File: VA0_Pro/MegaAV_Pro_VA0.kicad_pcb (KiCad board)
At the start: 4 copper layers, 50 x 50 mm, 180 parts, among them CN1 MD-90SM_MD2, P1 SMD_Conn_01x01, U1 CD4070, U2 74HCT123, U3 TS924, U4 THS7374, U5 ICS501, U6 TS922, U7 TS924, U8 AD723, U9 NCV8114ASN250T1G

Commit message: MegaAV VA0 CE PCBA updates
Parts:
- U6: footprint Package_SO:TSSOP-8_4.4x3mm_P0.65mm -> Package_SO:SO-8_3.9x4.9mm_P1.27mm
- moved R58 2.73 mm to (176.6, 105.0)
- moved C31 1.68 mm to (188.6, 107.6)
- moved U6 0.94 mm to (190.3, 104.4)
- moved C43 0.61 mm to (193.0, 109.3), turned to 180 degrees
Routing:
- net /V_REF: track 78.2 -> 72.2 mm
- net Net-(HPL_RES2-C): track 48.7 -> 45.2 mm
- net +5V: track 279.1 -> 276.0 mm
- net GND: track 55.0 -> 52.0 mm, vias 80 -> 79
- net /CV-OUT: track 7.29 -> 4.37 mm
- net Net-(C43-Pad1): track 2.33 -> 4.86 mm
- net Net-(C48-Pad2): track 4.20 -> 6.36 mm
- net /AUD-M: track 24.8 -> 22.8 mm
- net Net-(HPL_SL2-Pin_1): track 44.4 -> 43.1 mm
- net Net-(C33-Pad1): track 13.7 -> 14.9 mm
- net Net-(HPR_SL2-Pin_1): track 58.3 -> 57.2 mm
- net /AUD-L: track 23.2 -> 23.7 mm

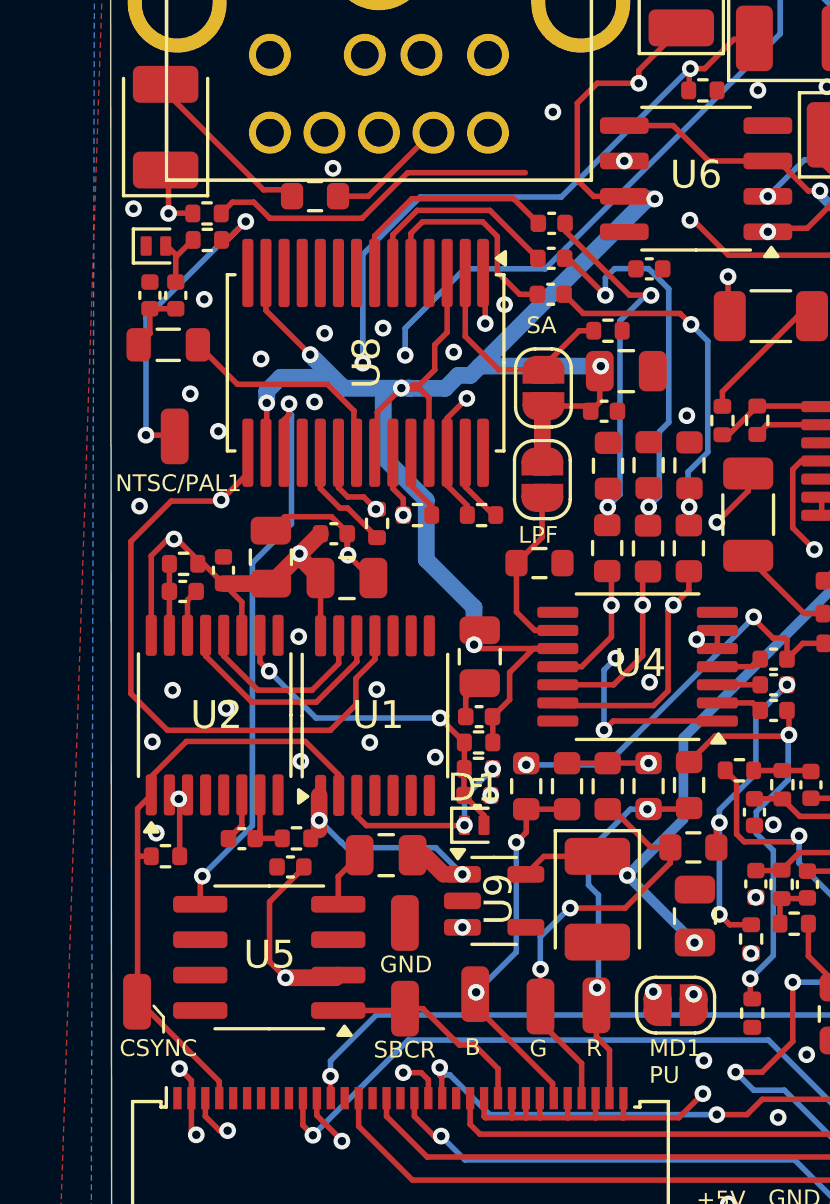
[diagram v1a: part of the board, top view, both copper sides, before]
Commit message: Fixed VA0 errors
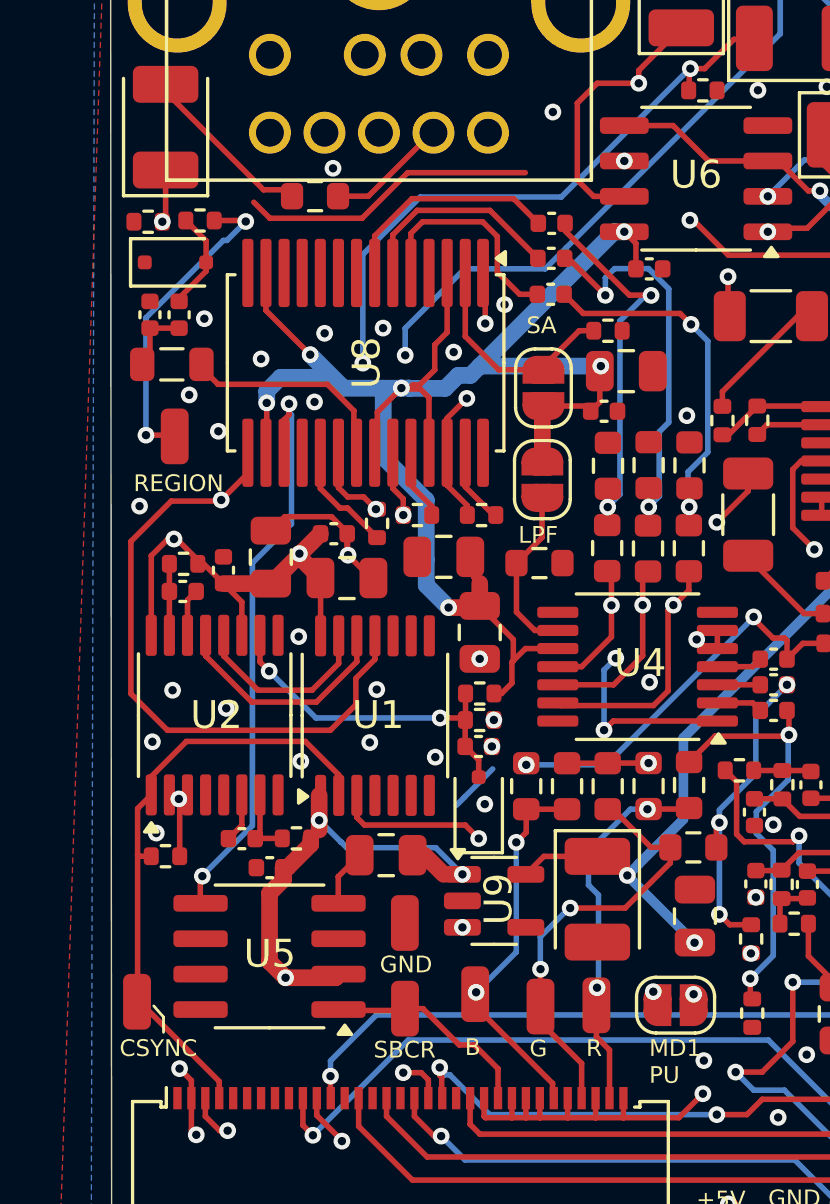
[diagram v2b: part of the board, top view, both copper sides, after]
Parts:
- added G***: LOGO, MyLibrary:RIP-Felix Logo(Small), B.Cu at (193.3, 140.9)
- C28: footprint Capacitor_SMD:C_0402_1005Metric -> Capacitor_SMD:C_0805_2012Metric
- D1, D2: footprint Diode_SMD:D_SOD-882 -> Diode_SMD:D_SOD-323F
- moved C28 5.87 mm to (181.3, 117.9)
- moved R68 2.13 mm to (170.6, 105.9), turned to 180 degrees
- moved C5 1.76 mm to (182.5, 124.7)
- moved R1 1.76 mm to (182.5, 123.8)
- moved R20 1.76 mm to (182.5, 122.8)
- moved D2 0.91 mm to (171.6, 107.4)
- moved C29 0.87 mm to (182.5, 120.7)
- moved R59 0.75 mm to (172.5, 105.9)
- moved C23 0.74 mm to (175.0, 129.1)
- moved L1 0.71 mm to (171.5, 111.0)
- moved C49 0.70 mm to (171.8, 109.3)
- moved C50 0.69 mm to (170.7, 109.3)
- moved D1 0.64 mm to (182.5, 126.9), turned to 90 degrees
- renumbered NTSC/PAL1 to REGION
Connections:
- net /NTSC/PAL renamed /REGION
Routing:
- net Net-(D1-K): track 7.23 -> 10.8 mm
- net Net-(D2-A): track 2.21 -> 3.65 mm
- net GND: track 52.0 -> 51.1 mm, vias 79 -> 80
- net Net-(D1-A): track 12.9 -> 12.3 mm
- net +5V: track 276.0 -> 276.6 mm
- net Net-(U8-CVBS_OUT): track 21.2 -> 20.6 mm
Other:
- board text added: "JUMPER SETTINGS: MD1 VA0-6.8: 1AC MD1 VA7, MD2 VA3: 2AC [-01, 2AF] MD2 VA0-1.8: 2 ACD [-01, 2AFD] MD2 VA2-2.3: 1B MD2 VA4: 2A MD3: 2AD REGION SELECT: Bridge PAL Or NTSC Jumper Bridge SA for PAL_M If you LIFTED RGB Legs: MD1PU HEADPHONE OUT: MD1 VA0-VA6.8: Y MD1 VA7, CDX, NOMAD, MEGA JET: Z NO HEADPHONE OUT: Y & SHORT HP P1 AND HP P2"
- board text added: "PRO"
- board text added: "rev. VA0"
- board text removed: "JUMPER SETTINGS: MD1 VA0-6.8: 1 A C MD1 VA7, MD2 VA3: 2 A C [-01, 2 A F] MD2 VA0-1.8: 2 A C D [-01, 2 A F D] MD2 VA2-2.3: 1 B MD2 VA4: 2 A MD3: 2 A D REGION SELECT: Bridge PAL Or NTSC Jumper Bridge SA for PAL_M If you LIFTED RGB Legs: MD1PU HEADPHONE OUT: MD1 VA0-VA6.8: Y MD1 VA7, CDX, NOMAD, MEGA JET: Z NO HEADPHONE OUT: Y & SHORT HP P1 AND HP P2"
- board text removed: "rev. VA1"
